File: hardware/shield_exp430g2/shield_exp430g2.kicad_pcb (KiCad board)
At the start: 2 copper layers, 58.7 x 51.2 mm, 49 parts, among them J1 Digital, J14 Conn_01x04_Male, J2 Digital, J9 Conn_02x13_Odd_Even, M1 Conn_01x02_Male, M1N Conn_01x02_Male, M2 Conn_01x02_Male, M2N Conn_01x02_Male, Q1 2N7002, Q2 2N7002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

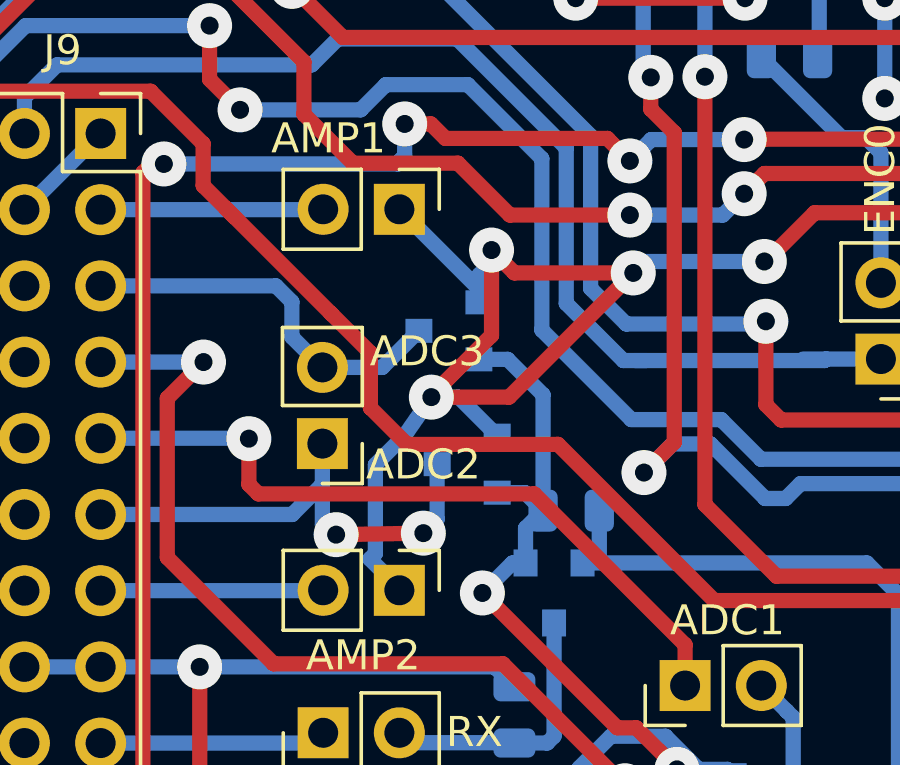
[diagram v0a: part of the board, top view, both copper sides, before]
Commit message: Added documentation files
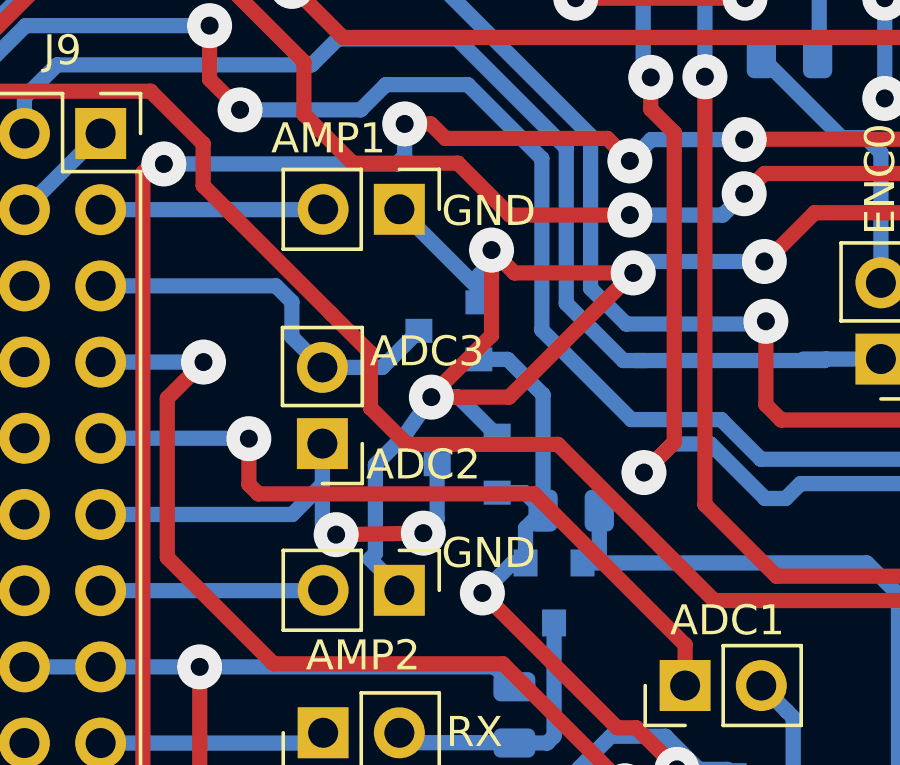
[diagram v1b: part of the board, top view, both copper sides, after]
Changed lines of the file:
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@@
   (general
     (thickness 1.6)
-    (drawings 11)
+    (drawings 13)
     (tracks 644)
     (zones 0)
@@
     )
   )
+  (gr_text GND (at 132.898 101.565) (layer F.SilkS)
+    (effects (font (size 1 1) (thickness 0.1)))
+  )
+  (gr_text GND (at 132.898 90.165) (layer F.SilkS)
+    (effects (font (size 1 1) (thickness 0.1)))
+  )
   (gr_text 3V3 (at 118.11 121.4247 90) (layer F.SilkS)
     (effects (font (size 1 1) (thickness 0.25)))
@@
   )
   (gr_text ADC2 (at 130.7211 98.6155) (layer F.SilkS)
-    (effects (font (size 1 1) (thickness 0.25)))
+    (effects (font (size 1 1) (thickness 0.15)))
   )
   (dimension 51.142939 (width 0.3) (layer F.SilkS)

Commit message: Added 3d Models
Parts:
- J1, J2: footprint Socket_Arduino_Uno:Socket_Strip_Arduino_1x10 -> Connector_PinHeader_2.54mm:PinHeader_1x10_P2.54mm_Vertical; moved to B.Cu
- turned J1 to 270 degrees
- turned J2 to 270 degrees

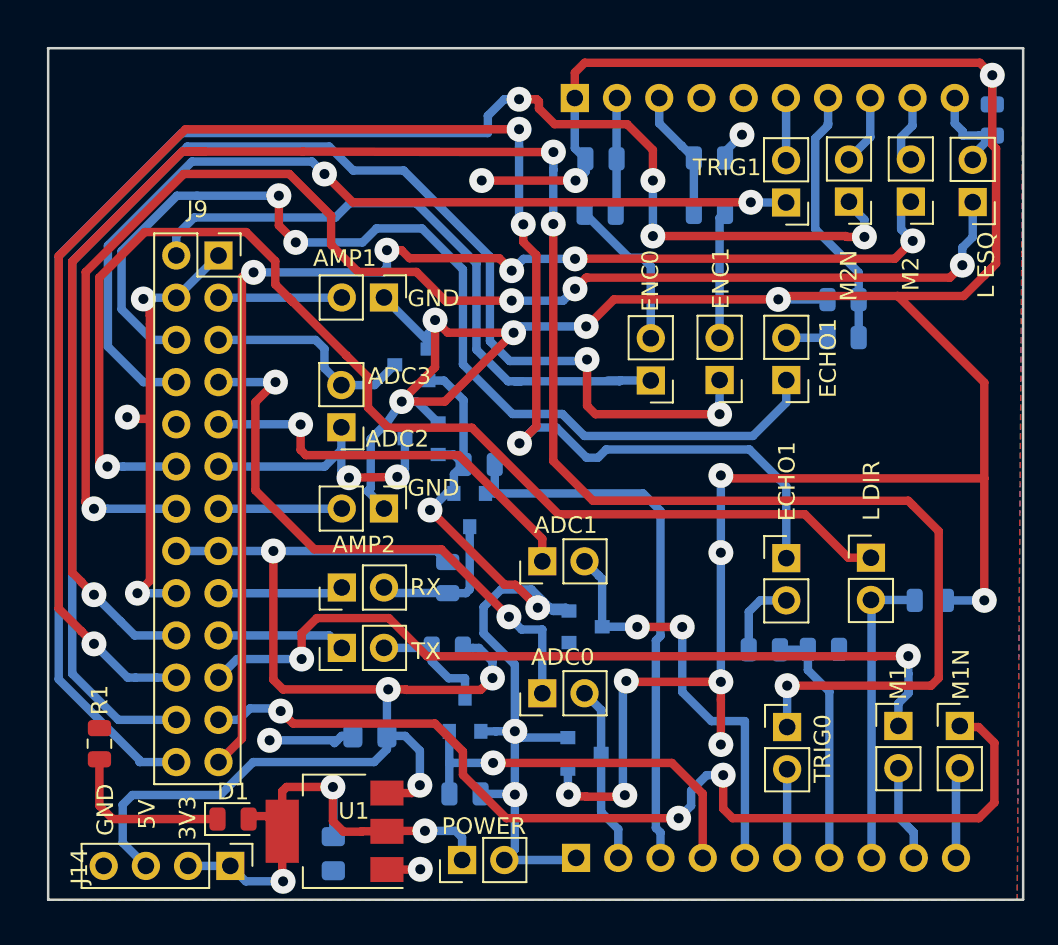
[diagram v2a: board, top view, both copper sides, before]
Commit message: Updated shield hardware, added uart protection!
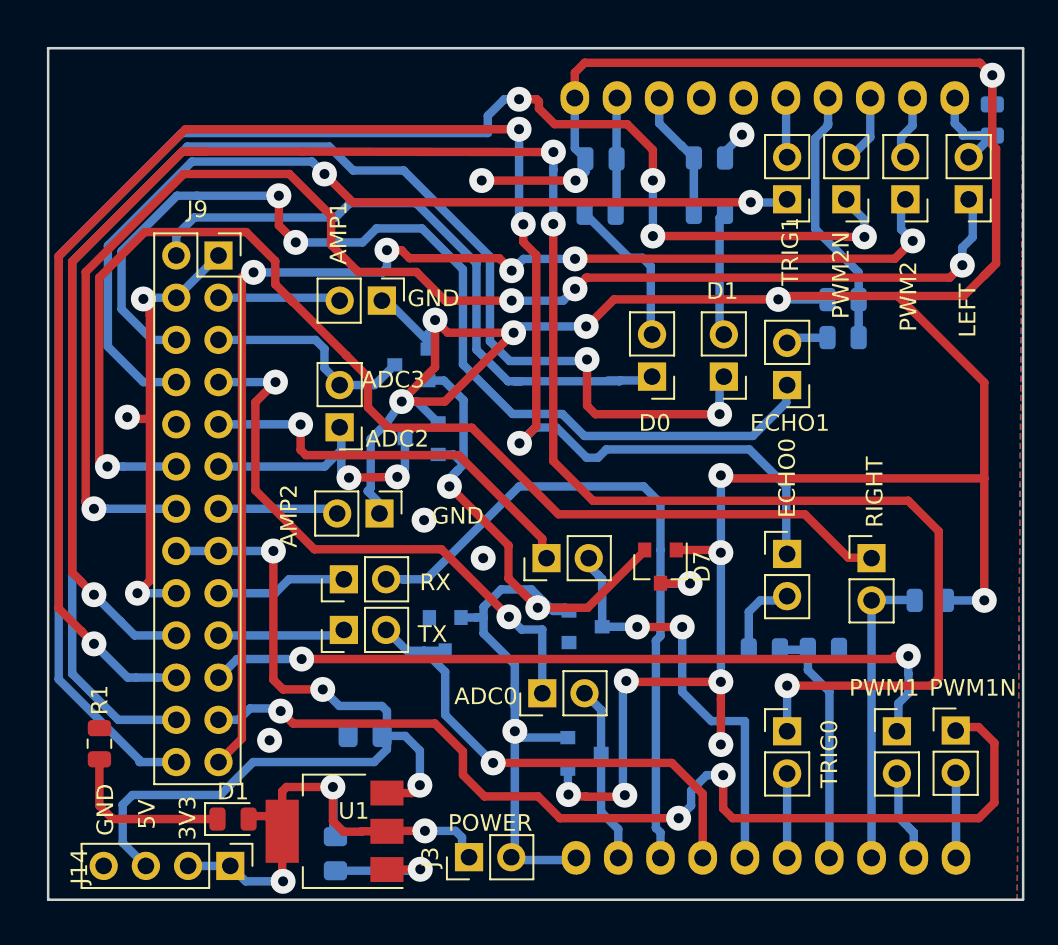
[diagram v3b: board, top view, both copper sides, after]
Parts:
- removed ADC0, ADC1, ADC3, AMP1, AMP2, ECHO1 (x2), ENC0, ENC1, M1, M1N, M2, M2N, POWER, RX, TRIG0, TRIG1, TX: Conn_01x02_Male, Connector_PinHeader_2.54mm:PinHeader_1x02_P2.54mm_Vertical
- removed L DIR: Conn_01x02_Male, Connector_PinHeader_2.54mm:PinHeader_1x02_P2.54mm_Vertical
- removed L ESQ: Conn_01x02_Male, Connector_PinHeader_2.54mm:PinHeader_1x02_P2.54mm_Vertical
- removed Q1, Q2: 2N7002, Package_TO_SOT_SMD:SOT-23
- removed R12, R13, R14, R15: 2k2, Resistor_SMD:R_0805_2012Metric
- added D6: BAT54S, Package_TO_SOT_SMD:SOT-23, B.Cu at (133.6, 110.4)
- added D7: BAT54S, Package_TO_SOT_SMD:SOT-23, F.Cu at (146.6, 106.3)
- added J10: Conn_01x02_Male, Connector_PinHeader_2.54mm:PinHeader_1x02_P2.54mm_Vertical, F.Cu at (154.2, 105.5)
- added J11: Conn_01x02_Male, Connector_PinHeader_2.54mm:PinHeader_1x02_P2.54mm_Vertical, F.Cu at (154.2, 116.2)
- added J12: Conn_01x02_Male, Connector_PinHeader_2.54mm:PinHeader_1x02_P2.54mm_Vertical, F.Cu at (154.2, 95.4)
- added J13: Conn_01x02_Male, Connector_PinHeader_2.54mm:PinHeader_1x02_P2.54mm_Vertical, F.Cu at (154.2, 84.2)
- added J15: Conn_01x02_Male, Connector_PinHeader_2.54mm:PinHeader_1x02_P2.54mm_Vertical, F.Cu at (160.8, 116.2)
- added J16: Conn_01x02_Male, Connector_PinHeader_2.54mm:PinHeader_1x02_P2.54mm_Vertical, F.Cu at (164.3, 116.2)
- added J17: Conn_01x02_Male, Connector_PinHeader_2.54mm:PinHeader_1x02_P2.54mm_Vertical, F.Cu at (161.3, 84.2)
- added J18: Conn_01x02_Male, Connector_PinHeader_2.54mm:PinHeader_1x02_P2.54mm_Vertical, F.Cu at (157.7, 84.2)
- added J19: Conn_01x02_Male, Connector_PinHeader_2.54mm:PinHeader_1x02_P2.54mm_Vertical, F.Cu at (159.3, 105.8)
- added J20: Conn_01x02_Male, Connector_PinHeader_2.54mm:PinHeader_1x02_P2.54mm_Vertical, F.Cu at (165.1, 84.2)
- added J21: Conn_01x02_Male, Connector_PinHeader_2.54mm:PinHeader_1x02_P2.54mm_Vertical, F.Cu at (146.1, 94.9)
- added J22: Conn_01x02_Male, Connector_PinHeader_2.54mm:PinHeader_1x02_P2.54mm_Vertical, F.Cu at (127.5, 110.1)
- added J23: Conn_01x02_Male, Connector_PinHeader_2.54mm:PinHeader_1x02_P2.54mm_Vertical, F.Cu at (127.5, 107.1)
- added J24: Conn_01x02_Male, Connector_PinHeader_2.54mm:PinHeader_1x02_P2.54mm_Vertical, F.Cu at (150.4, 94.9)
- added J3: Conn_01x02_Male, Connector_PinHeader_2.54mm:PinHeader_1x02_P2.54mm_Vertical, F.Cu at (135.0, 123.8)
- added J4: Conn_01x02_Male, Connector_PinHeader_2.54mm:PinHeader_1x02_P2.54mm_Vertical, F.Cu at (129.8, 90.3)
- added J5: Conn_01x02_Male, Connector_PinHeader_2.54mm:PinHeader_1x02_P2.54mm_Vertical, F.Cu at (129.6, 103.1)
- added J6: Conn_01x02_Male, Connector_PinHeader_2.54mm:PinHeader_1x02_P2.54mm_Vertical, F.Cu at (139.4, 113.9)
- added J7: Conn_01x02_Male, Connector_PinHeader_2.54mm:PinHeader_1x02_P2.54mm_Vertical, F.Cu at (139.7, 105.8)
- added J8: Conn_01x02_Male, Connector_PinHeader_2.54mm:PinHeader_1x02_P2.54mm_Vertical, F.Cu at (127.3, 97.9)
- J1, J2: footprint Connector_PinHeader_2.54mm:PinHeader_1x10_P2.54mm_Vertical -> Socket_Arduino_Uno:Socket_Strip_Arduino_1x10
- moved C1 0.29 mm to (128.8, 116.5)
- moved C2 0.13 mm to (127.0, 123.6)
- turned J1 to 0 degrees
- turned J2 to 0 degrees
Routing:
- net +5V: track 73.0 -> 51.6 mm, vias 4 -> 3
- net P1.1: track 34.0 -> 44.6 mm, vias 0 -> 1
- net Rx: track 9.03 -> 0.00 mm
- net Tx: track 7.30 -> 0.00 mm
- net P1.2: track 23.7 -> 29.8 mm
- net +3V3: track 57.2 -> 61.2 mm, vias 4 -> 3
- net GND: track 231.8 -> 234.1 mm, vias 22 -> 24
- net PWM1: track 49.3 -> 47.5 mm
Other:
- board text added: "ADC0"
- board text added: "ADC3"
- board text added: "AMP1"
- board text added: "AMP2"
- board text added: "D0"
- board text added: "D1"
- board text added: "ECHO0"
- board text added: "ECHO1"
- board text added: "LEFT"
- board text added: "POWER"
- board text added: "PWM1"
- board text added: "PWM1N"
- board text added: "PWM2"
- board text added: "PWM2N"
- board text added: "RIGHT"
- board text added: "RX"
- board text added: "TRIG0"
- board text added: "TRIG1"
- board text added: "TX"

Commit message: Added aligment holes
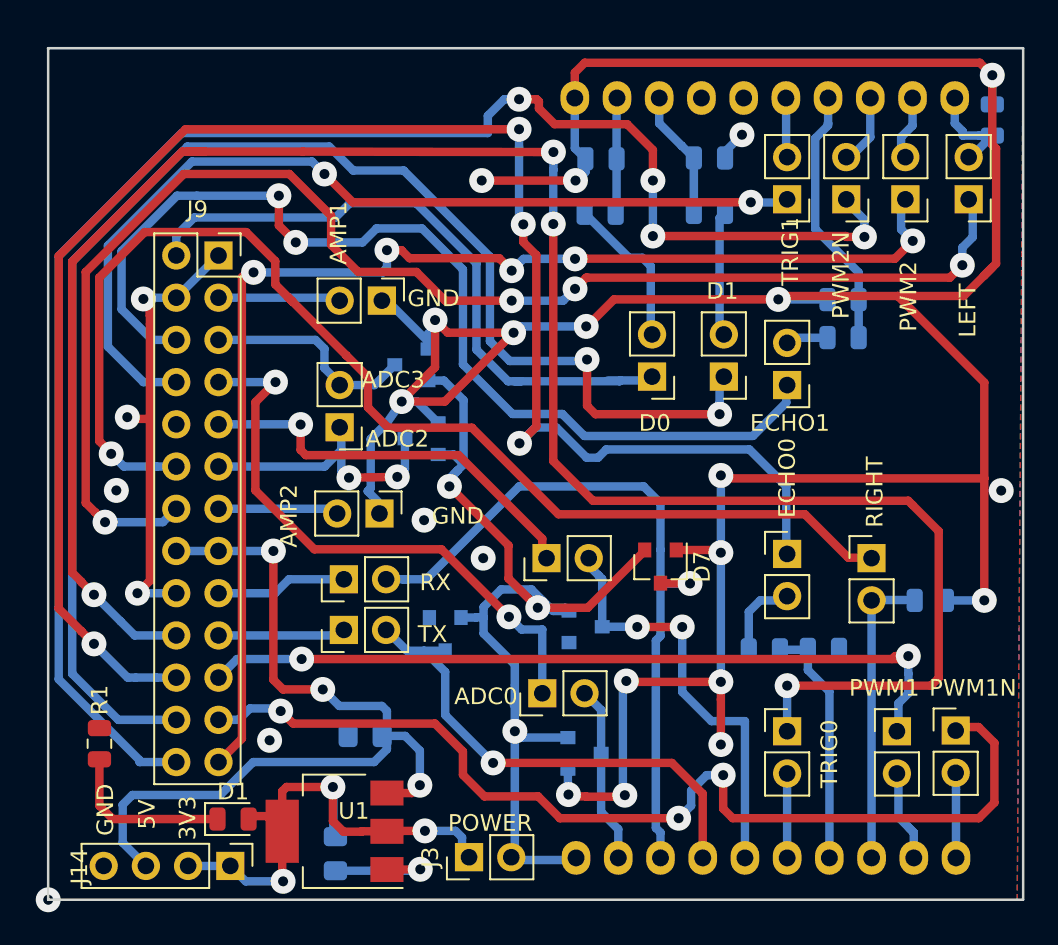
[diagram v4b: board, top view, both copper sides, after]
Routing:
- net R_TCRT: track 73.9 -> 73.1 mm
- net GND: vias 24 -> 26
- net (no net): vias 0 -> 1

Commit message: Updated g2553 board
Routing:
- net GND: track 234.1 -> 238.9 mm
- net R_TCRT: track 73.1 -> 74.5 mm
- net ADC0: track 35.0 -> 34.0 mm
- net P2.0: track 18.2 -> 18.9 mm
- net (no net): vias 1 -> 2
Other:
- net class Default: via_dia 1.5 -> 1.8

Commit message: Added diode
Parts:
- added D8: D_Schottky, Diode_SMD:D_SMB, B.Cu at (129.9, 113.6)
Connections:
- J9 pad 15: +5V -> +5VP
- J9 pad 16: +5V -> +5VP
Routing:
- net +5VP: track 0.00 -> 18.8 mm, vias 0 -> 2
- net +5V: track 51.6 -> 34.8 mm, vias 3 -> 1
- net Echo0: track 103.3 -> 111.5 mm
- net PWM1N: track 61.1 -> 64.5 mm
- net Net-(C2-Pad1): track 32.9 -> 34.3 mm
- net P1.2: track 29.8 -> 30.5 mm
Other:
- board text added: "3V3 POWER"
- board text removed: "POWER"
